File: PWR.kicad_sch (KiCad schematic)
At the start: 36 parts, among them J1 USB_B_Mini, J16 Conn_01x02_Pin, Q3 AO3401A, U2 XC6206P332MR, U4 MCP6001-OT, U5 AMS1117-3.3, U6 TP4057

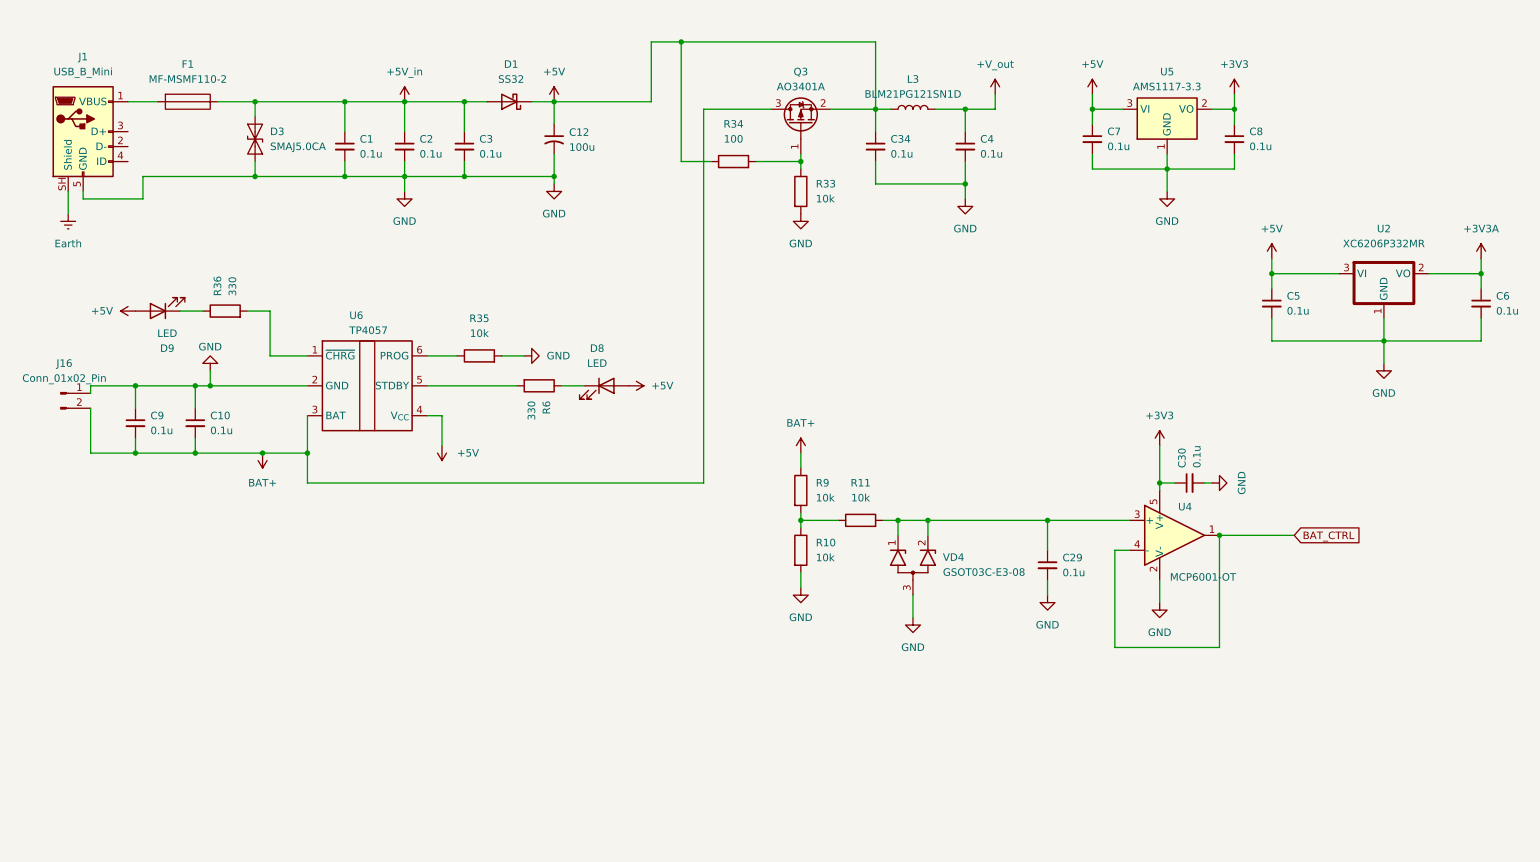
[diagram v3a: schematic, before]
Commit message: feat:убрал часть с батарейным питанием, убрал лишние элементы со старого проекта
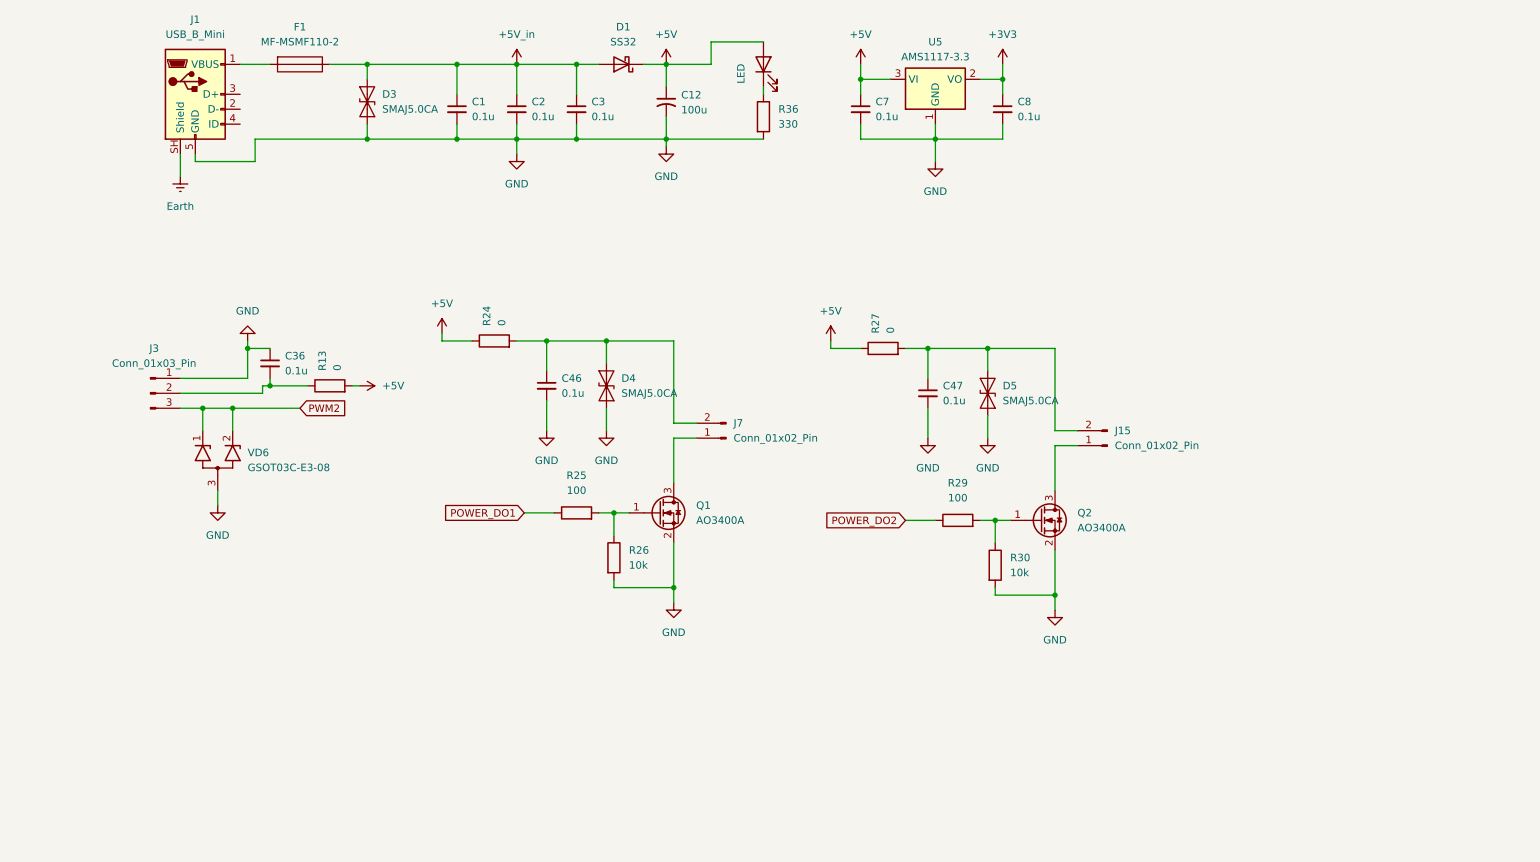
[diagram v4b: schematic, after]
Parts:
- removed C10, C29, C30, C34, C4, C5, C6, C9: 0.1u, Capacitor_SMD:C_0805_2012Metric_Pad1.18x1.45mm_HandSolder, symbol Device:C_Small
- removed D8: LED, LED_SMD:LED_0805_2012Metric_Pad1.15x1.40mm_HandSolder, symbol Device:LED
- removed J16: Conn_01x02_Pin, Connector_Hirose:Hirose_DF13-02P-1.25DSA_1x02_P1.25mm_Vertical, symbol Connector:Conn_01x02_Pin
- removed L3: BLM21PG121SN1D, Inductor_SMD:L_0805_2012Metric_Pad1.05x1.20mm_HandSolder, symbol Inductors:L
- removed Q3: AO3401A, Package_TO_SOT_SMD:SOT-23, symbol Transistor_FET:AO3401A
- removed R10, R11, R33, R35, R9: 10k, Resistor_SMD:R_0805_2012Metric_Pad1.20x1.40mm_HandSolder, symbol Device:R
- removed R34: 100, Resistor_SMD:R_0805_2012Metric_Pad1.20x1.40mm_HandSolder, symbol Device:R
- removed R6: 330, Resistor_SMD:R_0805_2012Metric_Pad1.20x1.40mm_HandSolder, symbol Device:R
- removed U2: XC6206P332MR, Package_TO_SOT_SMD:SOT-23, symbol Power_suply:XC6206P332MR
- removed U4: MCP6001-OT, Package_TO_SOT_SMD:SOT-23-5_HandSoldering, symbol Amplifier_Operational:MCP6001-OT
- removed U6: TP4057, Package_TO_SOT_SMD:TSOT-23-6, symbol Battery_Management:TP4057
- removed VD4: GSOT03C-E3-08, Package_TO_SOT_SMD:SOT-23, symbol TWS:GSOT03C-E3-08
- added C36, C46, C47: 0.1u, Capacitor_SMD:C_0805_2012Metric_Pad1.18x1.45mm_HandSolder, symbol Device:C_Small
- added D4, D5: SMAJ5.0CA, Diode_SMD:D_SMA, symbol Diode:SMAJ5.0CA
- added J15, J7: Conn_01x02_Pin, Connector_PinHeader_2.54mm:PinHeader_1x02_P2.54mm_Vertical, symbol Connector:Conn_01x02_Pin
- added J3: Conn_01x03_Pin, Connector_PinHeader_2.54mm:PinHeader_1x03_P2.54mm_Vertical, symbol Connector:Conn_01x03_Pin
- added Q1, Q2: AO3400A, Package_TO_SOT_SMD:SOT-23, symbol Transistor_FET:AO3400A
- added R13, R24, R27: 0, Resistor_SMD:R_0805_2012Metric_Pad1.20x1.40mm_HandSolder, symbol Device:R
- added R25, R29: 100, Resistor_SMD:R_0805_2012Metric_Pad1.20x1.40mm_HandSolder, symbol Device:R
- added R26, R30: 10k, Resistor_SMD:R_0805_2012Metric_Pad1.20x1.40mm_HandSolder, symbol Device:R
- added VD6: GSOT03C-E3-08, Package_TO_SOT_SMD:SOT-23, symbol TWS:GSOT03C-E3-08
- D9: footprint LED_SMD:LED_0805_2012Metric_Pad1.15x1.40mm_HandSolder -> LED_THT:LED_D3.0mm_Clear
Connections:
- net +5V: now also R13.2, R24.1, R27.1
- net GND: now also R36.2, C36.1, C46.2, C47.2, D4.1 (A1), D5.1 (A1), J3.1 (Pin_1), Q1.2 (S), Q2.2 (S), R26.2, R30.2, VD6.3 (A)
- new net: Q2.1 (G), R29.2, R30.1
- new net: J15.1 (Pin_1), Q2.3 (D)
- new net: Q1.1 (G), R25.2, R26.1
- new net: J7.1 (Pin_1), Q1.3 (D)
- new net: C36.2, J3.2 (Pin_2), R13.1
- new net: C46.1, D4.2 (A2), J7.2 (Pin_2), R24.2
- new net: C47.1, D5.2 (A2), J15.2 (Pin_2), R27.2
- new net POWER_DO1: R25.1
- new net POWER_DO2: R29.1
- new net PWM2: J3.3 (Pin_3), VD6.1 (K1), VD6.2 (K2)
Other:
- moved on the sheet: C1, C12, C2, C3, C7, C8, D1, D3, F1, J1, R36, U5

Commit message: feaat: добавлены светодиоды, кнопки и недостающие элементы защиты питания
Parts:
- removed R25, R29: 100, Resistor_SMD:R_0805_2012Metric_Pad1.20x1.40mm_HandSolder, symbol Device:R
- added C4: 0.1u, Capacitor_SMD:C_0805_2012Metric_Pad1.18x1.45mm_HandSolder, symbol Device:C_Small
- added D15: SMBJ5.0CA, Diode_SMD:D_SMB, symbol TVS_1:SMBJ5.0CA
- added R15: 10k, Resistor_SMD:R_0805_2012Metric_Pad1.20x1.40mm_HandSolder, symbol Device:R
- added R45, R46: 220, Resistor_SMD:R_0805_2012Metric_Pad1.20x1.40mm_HandSolder, symbol Device:R
- added U10: SRV05-4, Package_TO_SOT_SMD:SOT-23-6, symbol Power_Protection:SRV05-4
- R36: value 330 -> 220
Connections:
- net +5V: now also U10.5 (VP)
- net GND: now also C4.1, D15.2 (A2), R15.1, U10.2 (VN)
- net POWER_DO1: now also R45.1
- net POWER_DO2: now also R46.1
- net at Q2.1 (G), R30.1: now also R46.2
- net at Q1.1 (G), R26.1: now also R45.2
- net Earth renamed PE
- net PE: now also C4.2, D15.1 (A1), R15.2
- new net D+: U10.1 (IO1)
- new net D-: U10.3 (IO2)
- no-connect marks 0 -> 2
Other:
- moved on the sheet: C1, C12, C2, C3, C36, C46, C47, C7, C8, D1, D3, D4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

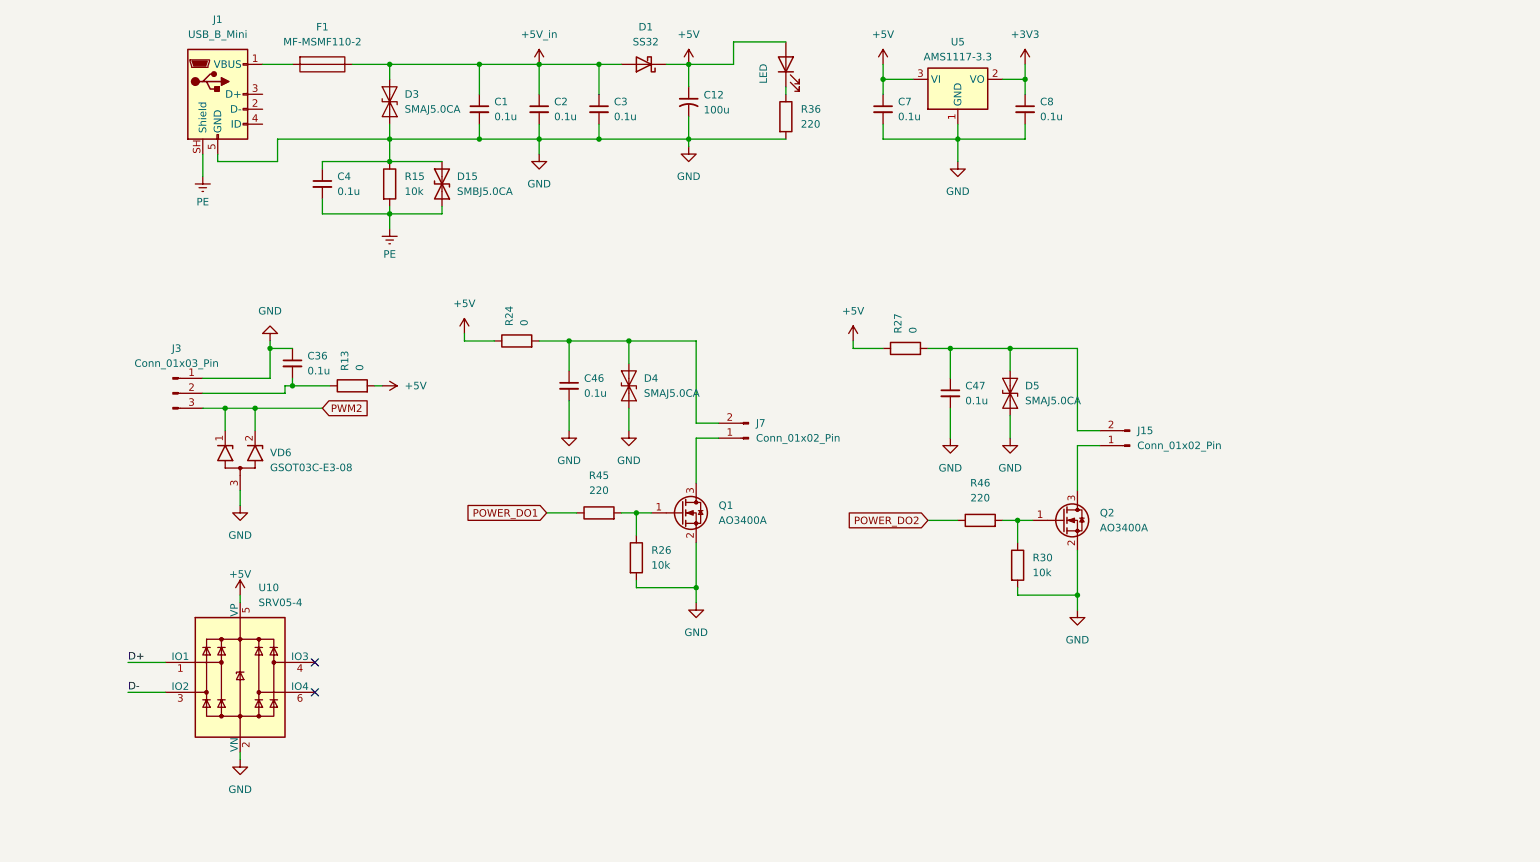
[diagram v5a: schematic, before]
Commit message: feat: добавлены глобальные линии связи, удалены линии связи со старого проекта
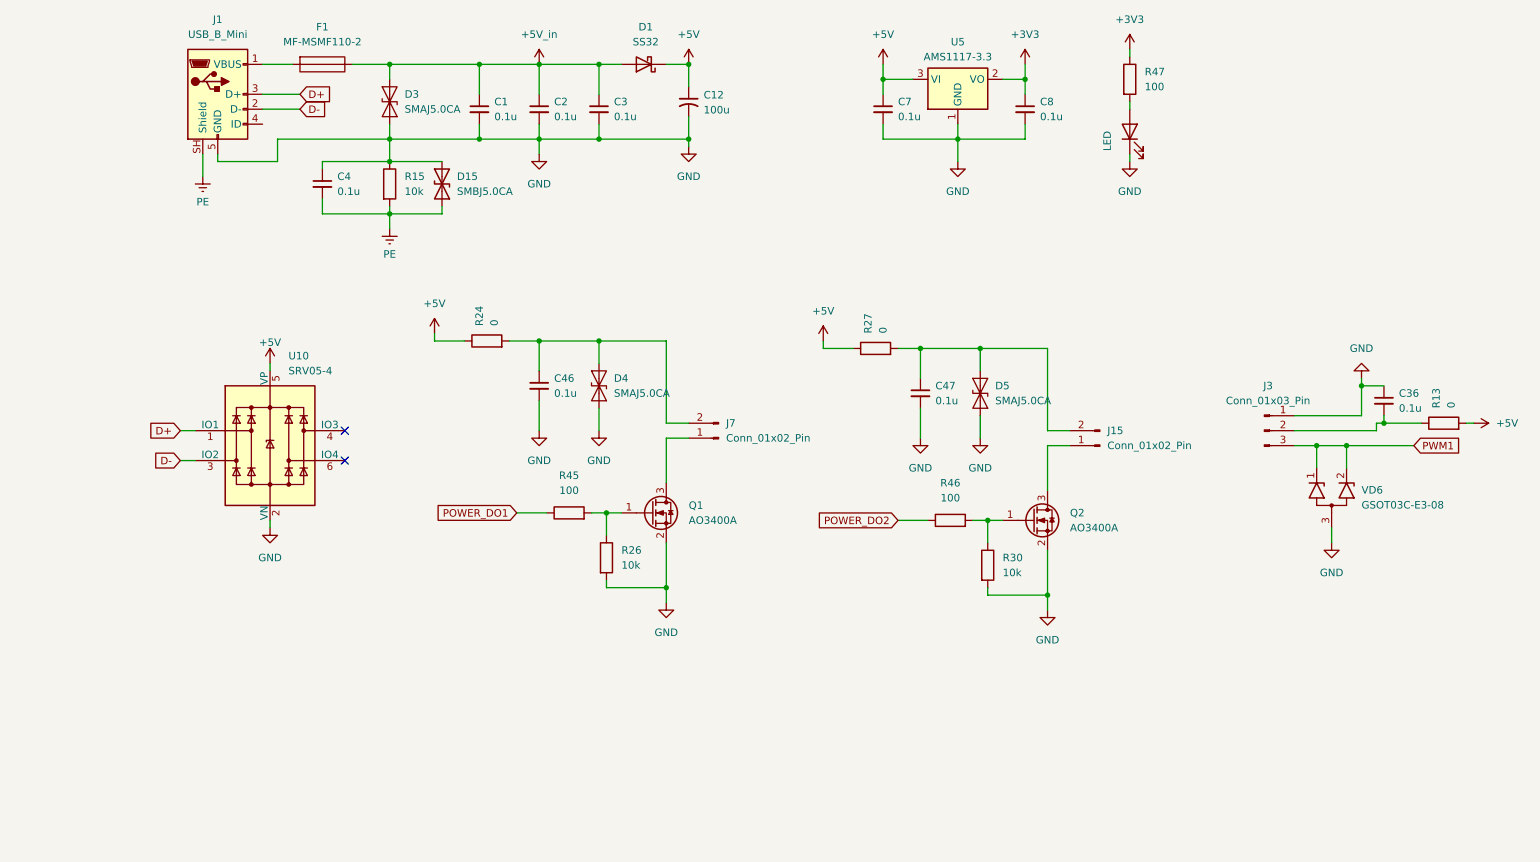
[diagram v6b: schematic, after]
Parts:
- removed R36: 220, Resistor_SMD:R_0805_2012Metric_Pad1.20x1.40mm_HandSolder, symbol Device:R
- added R47: 100, Resistor_SMD:R_0805_2012Metric_Pad1.20x1.40mm_HandSolder, symbol Device:R
- R45, R46: value 220 -> 100
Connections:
- net +3V3: now also R47.1
- net +5V: no longer D9.2 (A)
- net D+: now also J1.3 (D+)
- net D-: now also J1.2 (D-)
- net GND: now also D9.1 (K)
- net PWM2 renamed PWM1
- new net: D9.2 (A), R47.2
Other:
- moved on the sheet: C36, C46, C47, D4, D5, J15, J3, J7, Q1, Q2, R13, R24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

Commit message: feat: добавлены связи цифровых линий с МК
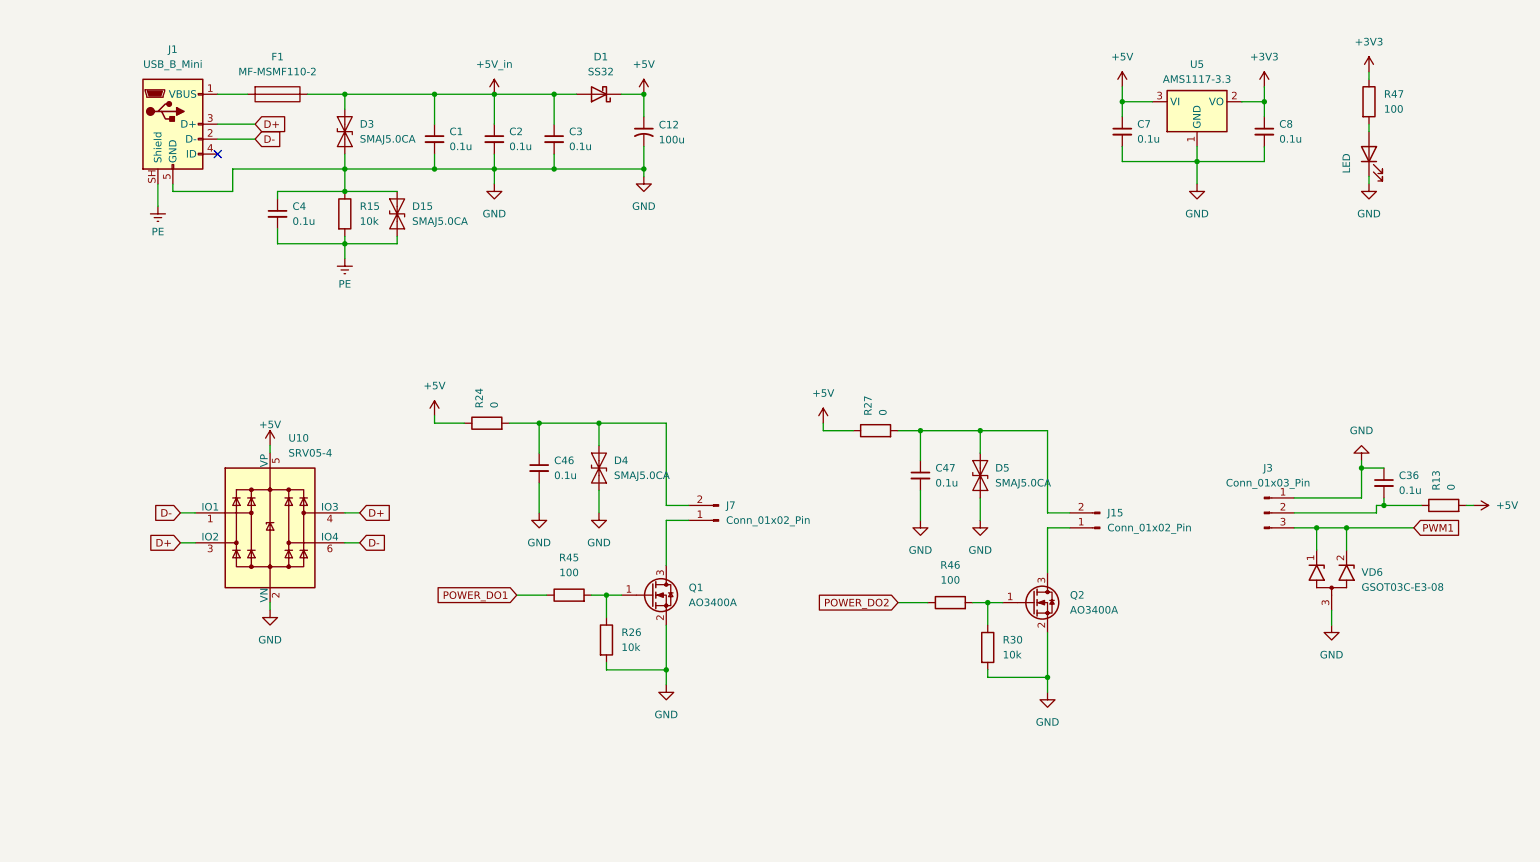
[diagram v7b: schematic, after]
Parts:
- removed D15: SMBJ5.0CA, Diode_SMD:D_SMB, symbol TVS_1:SMBJ5.0CA
- added D15: SMAJ5.0CA, Diode_SMD:D_SMA, symbol Diode:SMAJ5.0CA
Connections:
- net D+: now also U10.3 (IO2), U10.4 (IO3); no longer U10.1 (IO1)
- net D-: now also U10.1 (IO1), U10.6 (IO4); no longer U10.3 (IO2)
- net GND: now also D15.2 (A2)
- net PE: now also D15.1 (A1)
- no-connect marks 2 -> 1
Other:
- moved on the sheet: C1, C12, C2, C3, C36, C4, C46, C47, C7, C8, D1, D3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

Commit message: feat: добавлен дополнительный разъём для питания
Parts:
- added C5, C6, C9: 0.1u, Capacitor_SMD:C_0805_2012Metric_Pad1.18x1.45mm_HandSolder, symbol Device:C_Small
- added D2: SS32, Diode_SMD:D_SMA, symbol Diode:SS32
- added D20: SMAJ5.0CA, Diode_SMD:D_SMA, symbol Diode:SMAJ5.0CA
- added J2: Conn_01x03_Pin, Connector_JST:JST_NV_B03P-NV_1x03_P5.00mm_Vertical, symbol Connector:Conn_01x03_Pin
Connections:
- net +5V: now also D2.1 (K)
- net +5V_in: now also C5.1, C6.1, C9.1, D2.2 (A), D20.2 (A2), J2.1 (Pin_1)
- net GND: now also C5.2, C6.2, C9.2, D20.1 (A1), J2.2 (Pin_2)
- net PE: now also J2.3 (Pin_3)
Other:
- moved on the sheet: C36, C46, C47, C7, C8, D4, D5, J15, J3, J7, Q1, Q2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
